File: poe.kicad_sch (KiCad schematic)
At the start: 85 parts, among them Q1 FDMC2523P, Q2 FDMS86255, Q3 CSD17510Q5A, Q4 BCX56, Q5 CSD17510Q5A, T1 Transformer_Wurth_749119550, U20 TPS23734, U21 TCMT1107, U22 TL431CDBVR

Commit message: Add and assign footprint for PoE transformer
We use Wuerth 749119550 as PoE transformer. Add and assign the footprint
for it.

Signed-off-by: Stefan Agner <stefan@agner.ch>
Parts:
- T1: footprint LightBlue:Transformer_EPQ-13 -> LightBlue:Transformer_Wuerth_749119550
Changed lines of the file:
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@@
     (property "Reference" "T1" (id 0) (at 199.39 31.0958 0))
     (property "Value" "Transformer_Wurth_749119550" (id 1) (at 199.39 33.3945 0))
-    (property "Footprint" "LightBlue:Transformer_EPQ-13" (id 2) (at 199.39 45.72 0)
+    (property "Footprint" "LightBlue:Transformer_Wuerth_749119550" (id 2) (at 199.39 45.72 0)
       (effects (font (size 1.27 1.27)) hide)
     )

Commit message: [WIP] PCB commit
Signed-off-by: Dominik Sliwa <dominik@sliwa.io>
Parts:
- D18, D24: value B3100-13-F -> B2100-13-F; footprint Diode_SMD:D_SMC -> Diode_SMD:D_SMB
- R52: footprint Resistor_SMD:R_0402_1005Metric -> Resistor_SMD:R_0805_2012Metric
- TP1: footprint TestPoint:TestPoint_Pad_D2.0mm -> TestPoint:TestPoint_Pad_D1.0mm
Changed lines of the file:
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@@
     (property "Reference" "TP1" (id 0) (at 59.7535 132.9498 90))
     (property "Value" "TestPoint" (id 1) (at 59.7535 136.5185 90))
-    (property "Footprint" "TestPoint:TestPoint_Pad_D2.0mm" (id 2) (at 60.325 129.54 0)
+    (property "Footprint" "TestPoint:TestPoint_Pad_D1.0mm" (id 2) (at 60.325 129.54 0)
       (effects (font (size 1.27 1.27)) hide)
     )
@@
       (effects (font (size 1.27 1.27)) (justify left))
     )
-    (property "Footprint" "Resistor_SMD:R_0402_1005Metric" (id 2) (at 182.88 127.635 0)
+    (property "Footprint" "Resistor_SMD:R_0805_2012Metric" (id 2) (at 182.88 127.635 0)
       (effects (font (size 1.27 1.27)) hide)
     )
@@
     (in_bom yes) (on_board yes)
     (property "Reference" "D18" (id 0) (at 92.71 170.5802 0))
-    (property "Value" "B3100-13-F" (id 1) (at 93.98 172.092 0))
-    (property "Footprint" "Diode_SMD:D_SMC" (id 2) (at 92.71 173.99 0)
+    (property "Value" "B2100-13-F" (id 1) (at 93.98 172.092 0))
+    (property "Footprint" "Diode_SMD:D_SMB" (id 2) (at 92.71 173.99 0)
       (effects (font (size 1.27 1.27)) hide)
     )
@@
     (in_bom yes) (on_board yes)
     (property "Reference" "D24" (id 0) (at 226.06 79.7752 0))
-    (property "Value" "B3100-13-F" (id 1) (at 224.79 81.287 0))
-    (property "Footprint" "Diode_SMD:D_SMC" (id 2) (at 226.06 83.185 0)
-      (effects (font (size 1.27 1.27)) hide)
-    )
+    (property "Value" "B2100-13-F" (id 1) (at 224.79 81.287 0))
+    (property "Footprint" "Diode_SMD:D_SMB" (id 2) (at 226.06 83.185 0)
+      (effects (font (size 1.27 1.27)) hide)
+    )

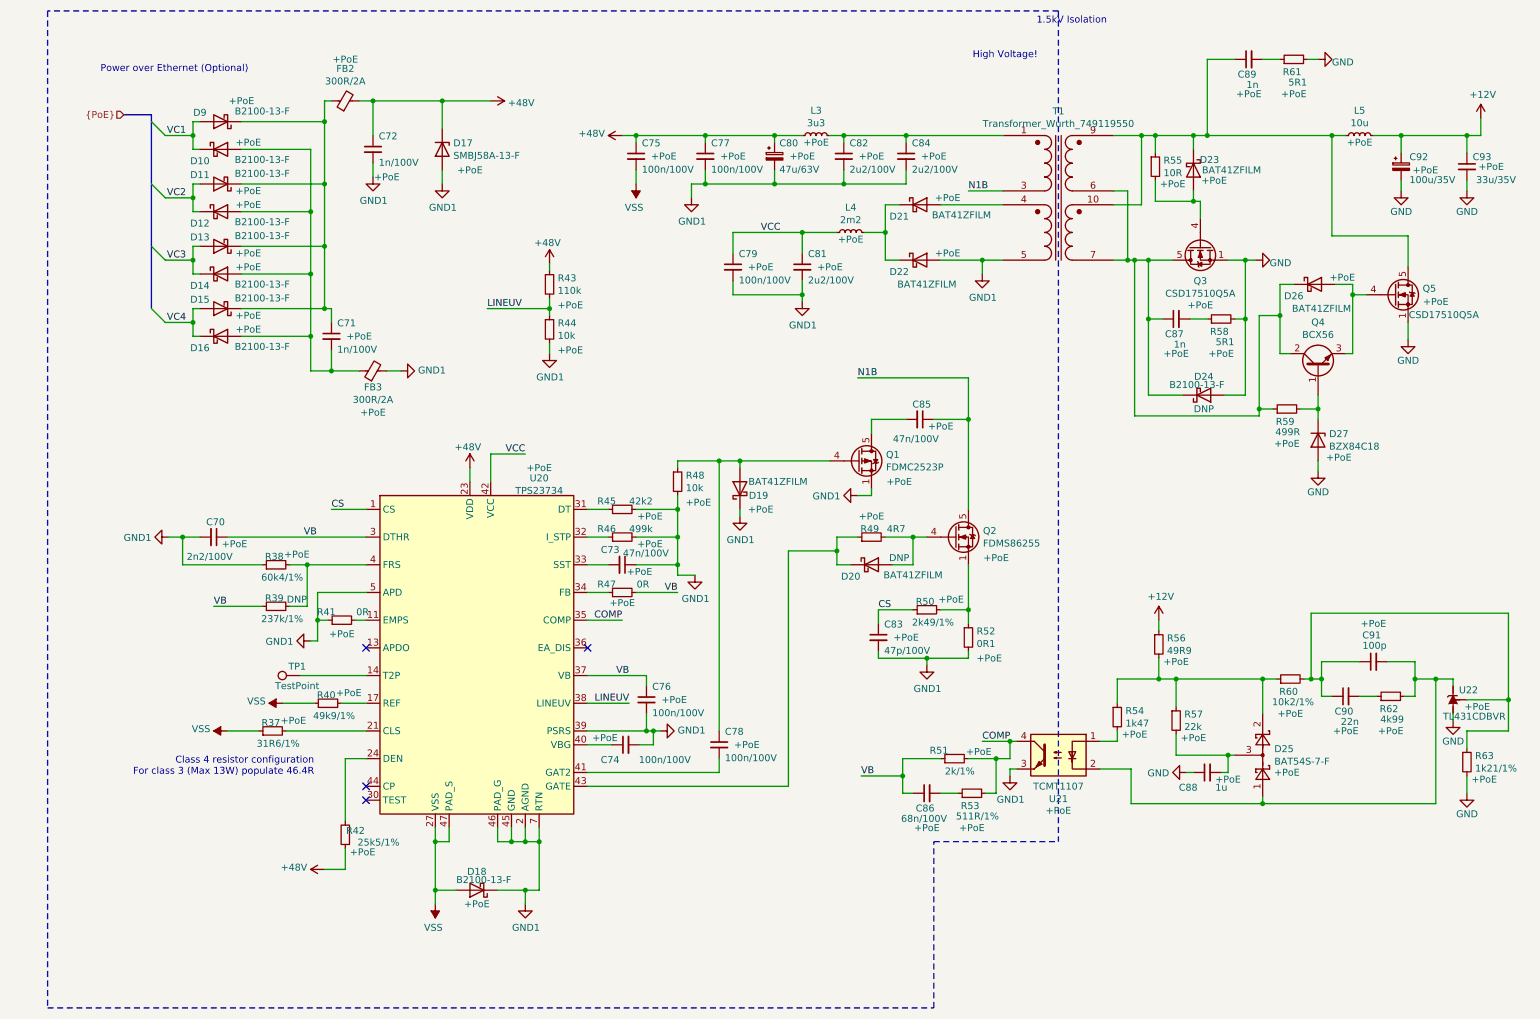
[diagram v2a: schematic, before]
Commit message: PCB[WIP]/SCH:
changes:
-more routing
-added poe negotiation disabled when +12V is present on the DC jack
-modified m.2 "holes"

Signed-off-by: Dominik Sliwa <dominik@sliwa.io>
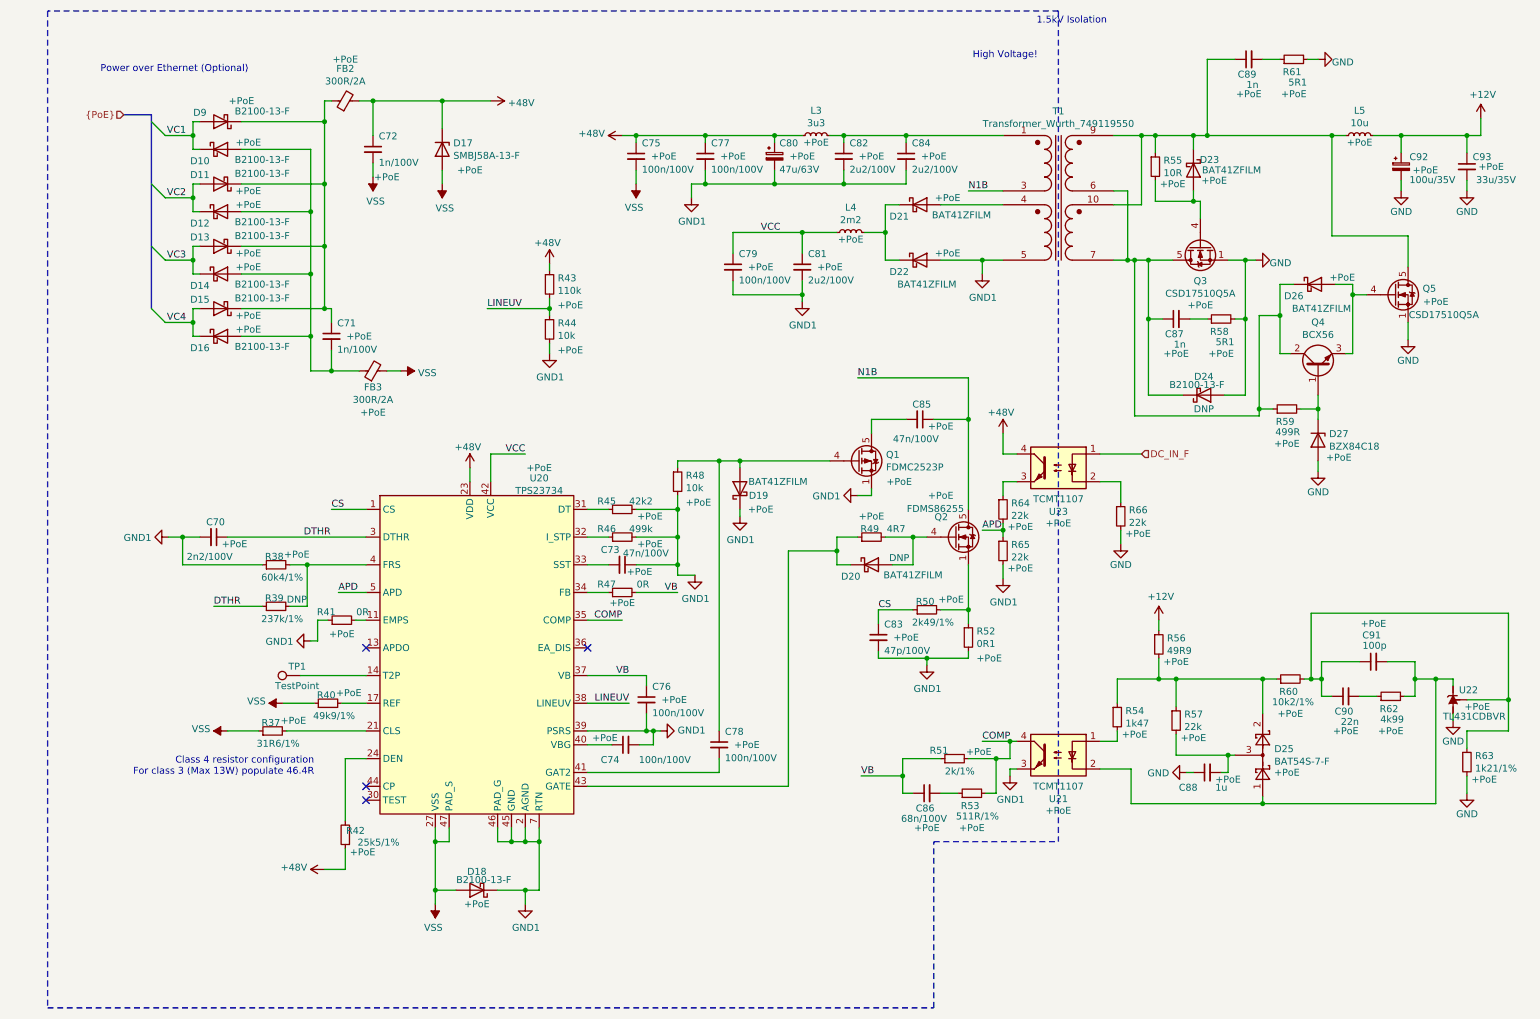
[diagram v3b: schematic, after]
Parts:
- added R64, R65, R66: 22k, Resistor_SMD:R_0402_1005Metric, symbol Device:R_Small
- added U23: TCMT1107, Package_SO:SOP-4_4.4x2.6mm_P1.27mm, symbol Isolator:TCMT1107
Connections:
- net +48V: now also U23.4
- net GND: now also R66.2
- net GND1: now also R65.2; no longer C72.2, D17.2 (A), FB3.2, U20.5 (APD)
- net VB: no longer C70.1, R39.1, U20.3 (DTHR)
- net VSS: now also C72.2, D17.2 (A), FB3.2
- new net: R66.1, U23.2
- new net: R64.1, U23.3
- new net APD: R64.2, R65.1, U20.5 (APD)
- new net DC_IN_F: U23.1
- new net DTHR: C70.1, R39.1, U20.3 (DTHR)

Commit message: Fix footprint of the PoE bulk capacitor C80
Use the correct footprint for the PoE bulk capacitor C80. The TI
evaluation module circuit uses a Panasonic EEE-FK1J470P bulk capacitor.
The series has other better suited alternatives like EEE-HA1J470UP, but
the F-size code seems to be a sensible choice.

Fixes: #1

Signed-off-by: Stefan Agner <stefan@agner.ch>
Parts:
- C80: footprint Capacitor_SMD:C_0805_2012Metric -> Capacitor_SMD:C_Elec_8x10.2; Manufacturer (none) -> Panasonic Electronic Components; PartNumber (none) -> EEE-HA1J470UP
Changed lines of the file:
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@@
       (effects (font (size 1.27 1.27)) (justify left))
     )
-    (property "Footprint" "Capacitor_SMD:C_0805_2012Metric" (id 2) (at 147.32 39.37 0)
+    (property "Footprint" "Capacitor_SMD:C_Elec_8x10.2" (id 2) (at 147.32 39.37 0)
       (effects (font (size 1.27 1.27)) hide)
     )
@@
     )
     (property "Config" "+PoE" (id 4) (at 152.4 39.37 0))
+    (property "Manufacturer" "Panasonic Electronic Components" (id 5) (at 147.32 39.37 0)
+      (effects (font (size 1.27 1.27)) hide)
+    )
+    (property "PartNumber" "EEE-HA1J470UP" (id 6) (at 147.32 39.37 0)
+      (effects (font (size 1.27 1.27)) hide)
+    )
     (pin "1")
     (pin "2")

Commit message: Specify charactristics of 0805 resistor in PoE
The reason we choose 0805 over 0402 is the required Wattage. Specify it
in the charactristics.

Signed-off-by: Stefan Agner <stefan@agner.ch>
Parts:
- R52: Characteristics (none) -> 0.1 Watt
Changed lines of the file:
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@@
     )
     (property "Config" "+PoE" (id 4) (at 186.69 131.445 0))
+    (property "Characteristics" "0.1 Watt" (id 5) (at 182.88 127.635 0)
+      (effects (font (size 1.27 1.27)) hide)
+    )
     (pin "1")
     (pin "2")

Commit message: Use the correct Part Number for the Würth PoE Transformer
Fixes: #2

Signed-off-by: Stefan Agner <stefan@agner.ch>
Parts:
- T1: PartNumber 749119550 -> 7491195112
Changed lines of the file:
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@@
       (effects (font (size 1.27 1.27)) hide)
     )
-    (property "PartNumber" "749119550" (id 6) (at 199.39 45.72 0)
+    (property "PartNumber" "7491195112" (id 6) (at 199.39 45.72 0)
       (effects (font (size 1.27 1.27)) hide)
     )
